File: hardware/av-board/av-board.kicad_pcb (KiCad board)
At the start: 6 copper layers, 94.6 x 69.4 mm, 234 parts, among them J1 RCA Y, J10 2x20 socket, J2 RCA Pb, J3 RCA Pr, J4 RCA L, J5 RCA R, J6 HDMI-001, J9 2x20 socket, SW1 TS-1187A-B-A-B, SW2 TS-1187A-B-A-B, U1 ADV7842KBCZ-5, U10 TPD4E05U06DQAR, U2 ADV7511KSTZ, U3 PCM1808PWR, U4 TLV62569DBVR, U5 TPS7A7001DDAR, U6 TPS7A7001DDAR, U7 TPS7A7001DDAR, U8 TPD4E05U06DQAR, U9 TPD4E05U06DQAR, Y1 28.63636MHz 20pF

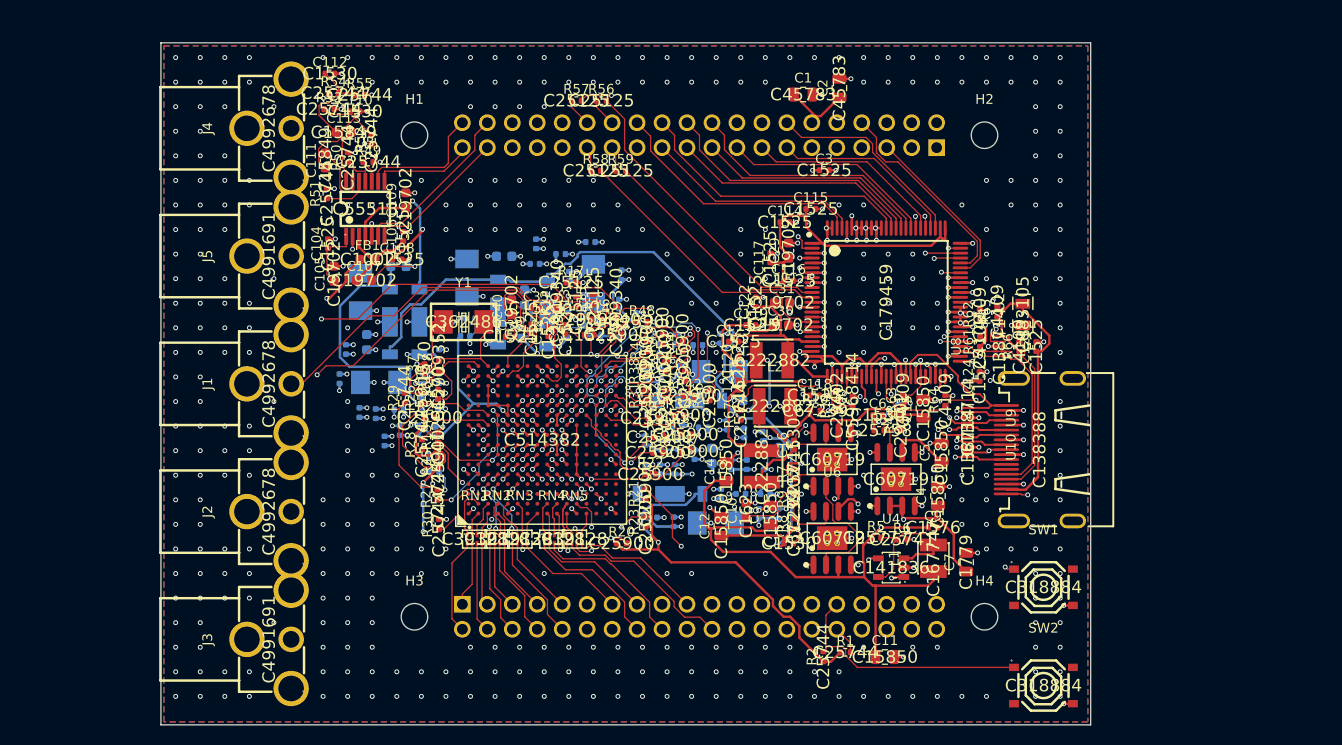
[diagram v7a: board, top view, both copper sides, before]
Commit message: TMDS refined on DeepPCB: pairs coupled, DRC clean
The routed board, refined: DeepPCB rerouted with only the locked fanout protected (any routed
track free to move), the rail planes kept clear of other wires and the stitching vias left out,
and routed D2 and D0 as pairs (81 % and 79 % coupled, 0.6 mm skew). mazeroute.py finished CK
and D1 with the N line following the P line (52 %, 59 %). Before, Freerouting had the four pairs
4-22 % coupled. Worst skew 3.7 mm (about 25 ps, HDMI allows about 100 ps). DRC: no errors.
R_EXT still has nothing switching near it.

- deeppcb.py: DEEPPCB_PROTECT_FILE (protect only the listed copper; DeepPCB otherwise protects
  all of it), DEEPPCB_PLANE_KEEPOUT (planes it receives can be cut by any net unless told),
  DEEPPCB_PAIR_WIDTH_MM/GAP_MM, DEEPPCB_NOVIA, DEEPPCB_FANOUT empty for none. A forced 0.25/0.2
  pair geometry made it route no TMDS at all: the connector's pins of a pair are 1 mm apart.
- sesgraft.py: one group of nets' copper from a session onto a routed board.
- mazeroute.py: a partner net to follow (a pair's other half); a track on any layer stands in a
  new via's way (four vias landed on an In3 track before).

Co-Authored-By: Claude Opus 5.5 <noreply@anthropic.com>
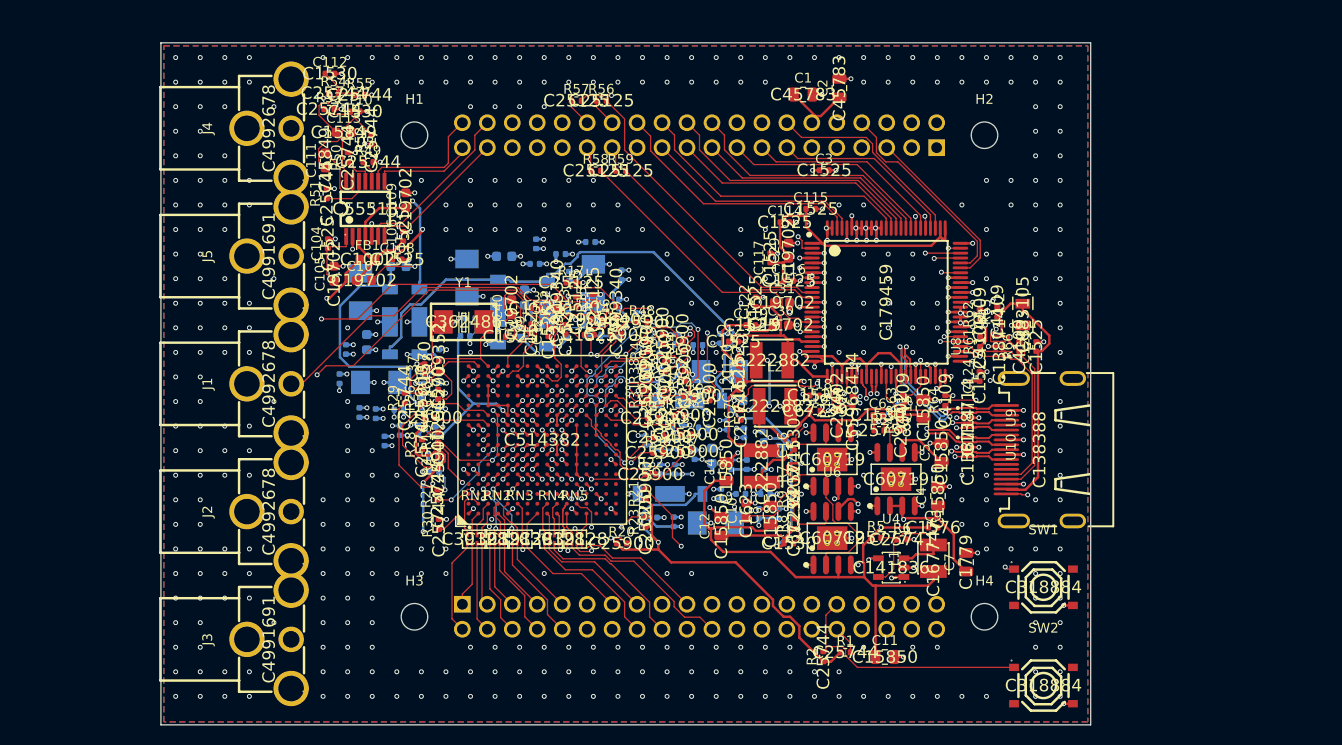
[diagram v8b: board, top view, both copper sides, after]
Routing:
- net GND: track 295.8 -> 310.8 mm, vias 646 -> 647
- net TMDS_D2_N: track 15.0 -> 19.8 mm
- net AV_VDD: track 19.0 -> 23.4 mm
- net AV_DVDDIO: track 46.2 -> 50.5 mm
- net TMDS_CK_P: track 21.9 -> 19.0 mm
- net TMDS_D1_N: track 15.2 -> 17.6 mm
- net TMDS_D2_P: track 16.9 -> 19.2 mm, vias 0 -> 2
- net AV_AVDD: track 34.3 -> 36.5 mm
- net TMDS_CK_N: track 21.3 -> 22.8 mm, vias 2 -> 3
- net TMDS_D0_N: track 19.7 -> 18.2 mm
- net TMDS_D1_P: track 15.4 -> 14.4 mm
- net TMDS_D0_P: track 16.8 -> 17.6 mm
